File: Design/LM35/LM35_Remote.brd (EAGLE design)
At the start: 16.2 x 52.1 mm, 6 parts

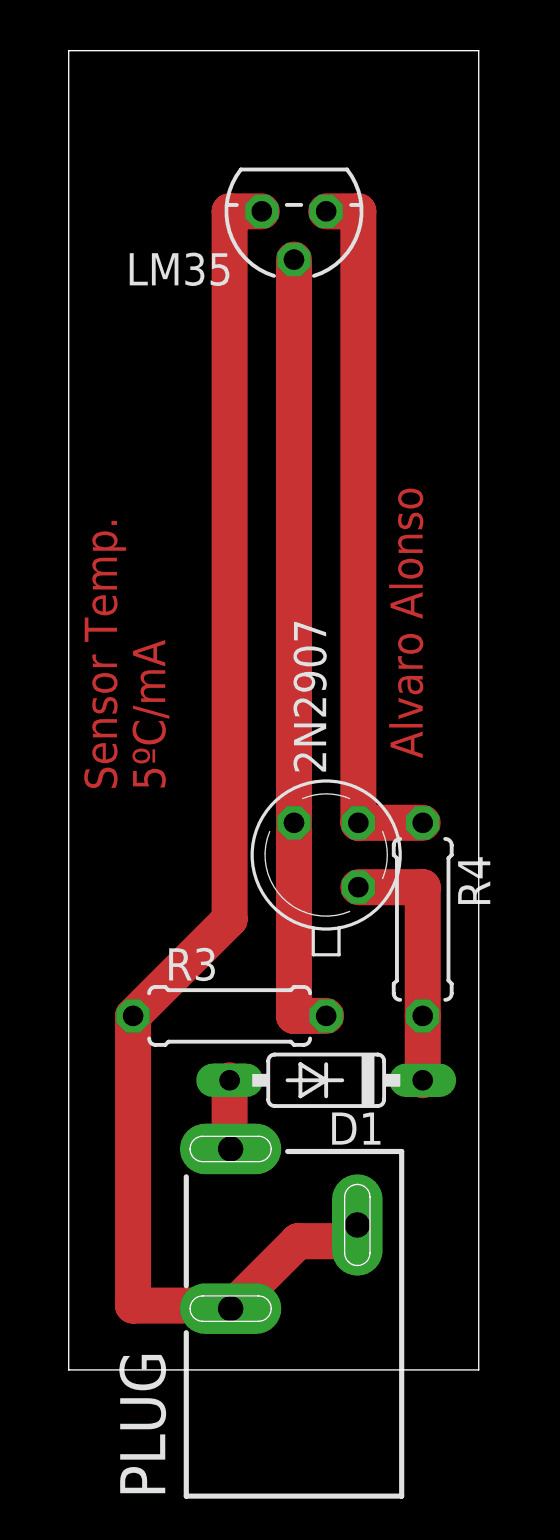
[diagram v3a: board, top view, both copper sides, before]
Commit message: Pequeñas modificaciones en el conector jack
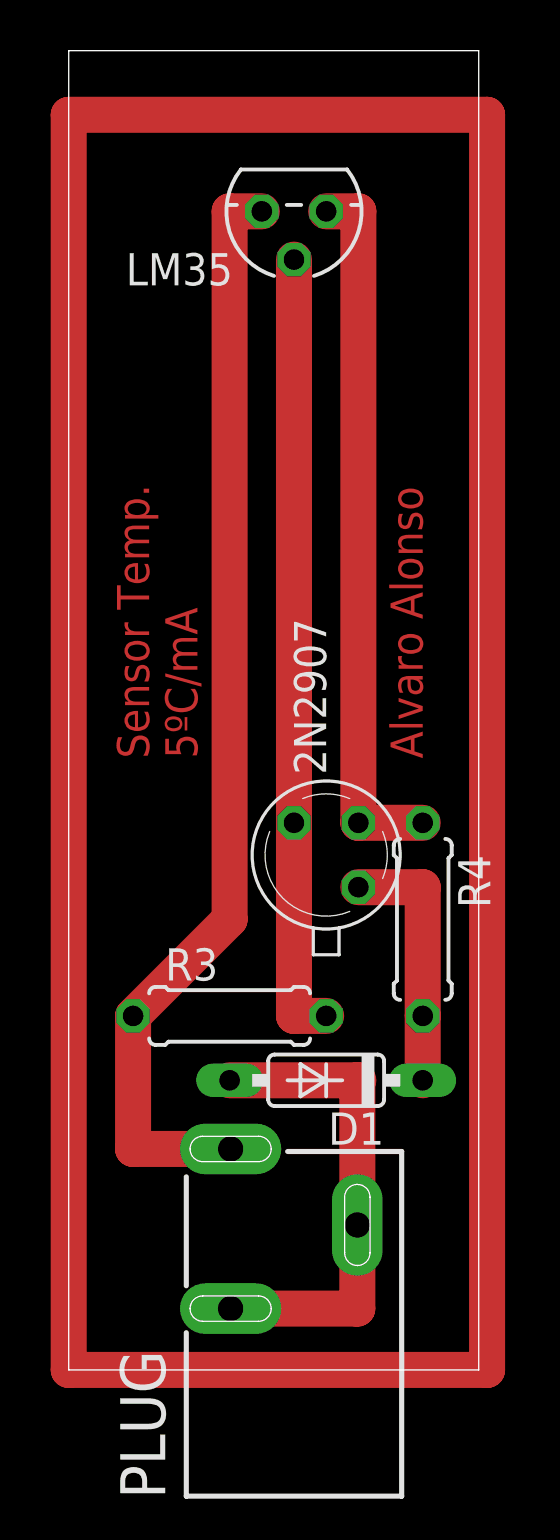
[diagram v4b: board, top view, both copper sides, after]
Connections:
- removed net N$5: D1.A, PLUG.1
- new net N$7: D1.A, PLUG.2, PLUG.3
- net N$4: now also PLUG.1; no longer PLUG.2, PLUG.3
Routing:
- net N$6: track 0.00 -> 132.1 mm
- net N$7: track 0.00 -> 19.1 mm
- net N$4: track 56.8 -> 43.7 mm
- net N$5: track 2.75 -> 0.00 mm
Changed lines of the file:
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@@
 <layer number="27" name="tValues" color="7" fill="1" visible="yes" active="yes"/>
 <layer number="28" name="bValues" color="7" fill="1" visible="yes" active="yes"/>
-<layer number="29" name="tStop" color="7" fill="3" visible="yes" active="yes"/>
-<layer number="30" name="bStop" color="7" fill="6" visible="yes" active="yes"/>
-<layer number="31" name="tCream" color="7" fill="4" visible="yes" active="yes"/>
-<layer number="32" name="bCream" color="7" fill="5" visible="yes" active="yes"/>
-<layer number="33" name="tFinish" color="6" fill="3" visible="yes" active="yes"/>
-<layer number="34" name="bFinish" color="6" fill="6" visible="yes" active="yes"/>
-<layer number="35" name="tGlue" color="7" fill="4" visible="yes" active="yes"/>
-<layer number="36" name="bGlue" color="7" fill="5" visible="yes" active="yes"/>
-<layer number="37" name="tTest" color="7" fill="1" visible="yes" active="yes"/>
-<layer number="38" name="bTest" color="7" fill="1" visible="yes" active="yes"/>
-<layer number="39" name="tKeepout" color="4" fill="11" visible="yes" active="yes"/>
-<layer number="40" name="bKeepout" color="1" fill="11" visible="yes" active="yes"/>
-<layer number="41" name="tRestrict" color="4" fill="10" visible="yes" active="yes"/>
-<layer number="42" name="bRestrict" color="1" fill="10" visible="yes" active="yes"/>
-<layer number="43" name="vRestrict" color="2" fill="10" visible="yes" active="yes"/>
-<layer number="44" name="Drills" color="7" fill="1" visible="yes" active="yes"/>
-<layer number="45" name="Holes" color="7" fill="1" visible="yes" active="yes"/>
-<layer number="46" name="Milling" color="3" fill="1" visible="yes" active="yes"/>
-<layer number="47" name="Measures" color="7" fill="1" visible="yes" active="yes"/>
-<layer number="48" name="Document" color="7" fill="1" visible="yes" active="yes"/>
-<layer number="49" name="Reference" color="7" fill="1" visible="yes" active="yes"/>
-<layer number="51" name="tDocu" color="7" fill="1" visible="yes" active="yes"/>
-<layer number="52" name="bDocu" color="7" fill="1" visible="yes" active="yes"/>
+<layer number="29" name="tStop" color="7" fill="3" visible="no" active="yes"/>
+<layer number="30" name="bStop" color="7" fill="6" visible="no" active="yes"/>
+<layer number="31" name="tCream" color="7" fill="4" visible="no" active="yes"/>
+<layer number="32" name="bCream" color="7" fill="5" visible="no" active="yes"/>
+<layer number="33" name="tFinish" color="6" fill="3" visible="no" active="yes"/>
+<layer number="34" name="bFinish" color="6" fill="6" visible="no" active="yes"/>
+<layer number="35" name="tGlue" color="7" fill="4" visible="no" active="yes"/>
+<layer number="36" name="bGlue" color="7" fill="5" visible="no" active="yes"/>
+<layer number="37" name="tTest" color="7" fill="1" visible="no" active="yes"/>
+<layer number="38" name="bTest" color="7" fill="1" visible="no" active="yes"/>
+<layer number="39" name="tKeepout" color="4" fill="11" visible="no" active="yes"/>
+<layer number="40" name="bKeepout" color="1" fill="11" visible="no" active="yes"/>
+<layer number="41" name="tRestrict" color="4" fill="10" visible="no" active="yes"/>
+<layer number="42" name="bRestrict" color="1" fill="10" visible="no" active="yes"/>
+<layer number="43" name="vRestrict" color="2" fill="10" visible="no" active="yes"/>
+<layer number="44" name="Drills" color="7" fill="1" visible="no" active="yes"/>
+<layer number="45" name="Holes" color="7" fill="1" visible="no" active="yes"/>
+<layer number="46" name="Milling" color="3" fill="1" visible="no" active="yes"/>
+<layer number="47" name="Measures" color="7" fill="1" visible="no" active="yes"/>
+<layer number="48" name="Document" color="7" fill="1" visible="no" active="yes"/>
+<layer number="49" name="Reference" color="7" fill="1" visible="no" active="yes"/>
+<layer number="51" name="tDocu" color="7" fill="1" visible="no" active="yes"/>
+<layer number="52" name="bDocu" color="7" fill="1" visible="no" active="yes"/>
 <layer number="90" name="Modules" color="5" fill="1" visible="no" active="no"/>
 <layer number="91" name="Nets" color="2" fill="1" visible="no" active="no"/>
@@
 <wire x1="18.72" y1="58.41" x2="2.54" y2="58.41" width="0" layer="20"/>
 <wire x1="2.54" y1="58.41" x2="2.54" y2="6.35" width="0" layer="20"/>
-<text x="6.35" y="29.21" size="1.27" layer="1" ratio="6" rot="R90">Sensor Temp.
+<text x="7.62" y="30.48" size="1.27" layer="1" ratio="6" rot="R90">Sensor Temp.
 5ºC/mA</text>
 <text x="16.51" y="30.48" size="1.27" layer="1" ratio="6" rot="R90">Alvaro Alonso</text>
@@
 <contactref element="R3" pad="1"/>
 <contactref element="LM35" pad="3"/>
-<contactref element="PLUG" pad="2"/>
-<contactref element="PLUG" pad="3"/>
-<wire x1="13.97" y1="12.07" x2="13.93" y2="12.07" width="1.4224" layer="1"/>
-<wire x1="13.93" y1="12.07" x2="13.93" y2="11.43" width="1.4224" layer="1"/>
-<wire x1="8.89" y1="8.77" x2="8.93" y2="8.77" width="1.4224" layer="1"/>
-<wire x1="13.93" y1="11.43" x2="11.59" y2="11.43" width="1.4224" layer="1"/>
-<wire x1="11.59" y1="11.43" x2="8.93" y2="8.77" width="1.4224" layer="1"/>
 <wire x1="10.16" y1="52.07" x2="8.89" y2="52.07" width="1.4224" layer="1"/>
 <wire x1="8.89" y1="52.07" x2="8.89" y2="24.13" width="1.4224" layer="1"/>
 <wire x1="8.89" y1="24.13" x2="5.08" y2="20.32" width="1.4224" layer="1"/>
-<wire x1="5.08" y1="20.32" x2="5.08" y2="8.89" width="1.4224" layer="1"/>
-<wire x1="5.08" y1="8.89" x2="8.93" y2="8.89" width="1.4224" layer="1"/>
-<wire x1="8.93" y1="8.89" x2="8.93" y2="8.77" width="1.4224" layer="1"/>
-</signal>
-<signal name="N$5">
+<contactref element="PLUG" pad="1"/>
+<wire x1="8.93" y1="15.07" x2="5.08" y2="15.07" width="1.4224" layer="1"/>
+<wire x1="5.08" y1="15.07" x2="5.08" y2="20.32" width="1.4224" layer="1"/>
+</signal>
+<signal name="N$6">
+<wire x1="2.54" y1="55.88" x2="19.05" y2="55.88" width="1.4224" layer="1"/>
+<wire x1="19.05" y1="55.88" x2="19.05" y2="6.35" width="1.4224" layer="1"/>
+<wire x1="19.05" y1="6.35" x2="2.54" y2="6.35" width="1.4224" layer="1"/>
+<wire x1="2.54" y1="6.35" x2="2.54" y2="55.88" width="1.4224" layer="1"/>
+</signal>
+<signal name="N$7">
+<contactref element="PLUG" pad="3"/>
+<contactref element="PLUG" pad="2"/>
 <contactref element="D1" pad="A"/>
-<contactref element="PLUG" pad="1"/>
-<wire x1="8.93" y1="15.07" x2="8.89" y2="15.07" width="1.4224" layer="1"/>
-<wire x1="8.89" y1="15.07" x2="8.89" y2="17.78" width="1.4224" layer="1"/>
+<wire x1="8.89" y1="17.78" x2="13.93" y2="17.78" width="1.4224" layer="1"/>
+<wire x1="13.97" y1="17.78" x2="13.93" y2="17.78" width="1.4224" layer="1"/>
+<wire x1="13.93" y1="17.78" x2="13.93" y2="12.07" width="1.4224" layer="1"/>
+<wire x1="8.93" y1="8.77" x2="13.93" y2="8.77" width="1.4224" layer="1"/>
+<wire x1="13.93" y1="8.77" x2="13.93" y2="12.07" width="1.4224" layer="1"/>
 </signal>
 </signals>

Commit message: Fix Doc files
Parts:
- removed 2N2907: (no value), transistor:TO18
- removed PLUG: (no value), con-shiua-chyuan:SCD-014-A
- added 2N3906: (no value), transistor-neu-to92:TO92-EBC
- added JP1: (no value), pinhead:1X02
- moved LM35 40.7 mm to (8.89, 11.4)
- moved R3 14.5 mm to (5.08, 6.35), turned to 90 degrees
- moved R4 14.5 mm to (12.7, 10.2)
- moved D1 11.7 mm to (15.2, 6.35), turned to 270 degrees
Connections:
- removed net N$4: LM35.3, PLUG.1, R3.1
- removed net N$7: D1.A, PLUG.2, PLUG.3
- new net IN: D1.A, JP1.1
- new net OUT: JP1.2, LM35.3, R3.1
- net N$1: now also 2N3906.B; no longer 2N2907.2
- net N$2: now also 2N3906.C; no longer 2N2907.3
- net N$3: now also 2N3906.E; no longer 2N2907.1
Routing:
- net N$6: track 132.1 -> 0.00 mm
- net N$4: track 43.7 -> 0.00 mm
- net N$2: track 31.1 -> 6.95 mm
- net N$7: track 19.1 -> 0.00 mm
- net N$1: track 27.9 -> 11.4 mm
- net N$3: track 10.2 -> 5.85 mm
- net IN: track 0.00 -> 3.81 mm
- added copper zone on layer 16, net OUT
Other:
- board size 16.2 x 52.1 mm -> 17.4 x 16.5 mm
- board text removed: "Alvaro Alonso"
- board text removed: "Sensor Temp. 5ºC/mA"
